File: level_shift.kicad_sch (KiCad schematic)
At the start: 37 parts, among them U1701 SN74LVC8T245PWR, U1702 SN74LVC8T245PWR, U1703 SN74LVC8T245PWR, U1704 SN74AVC4T245PWR, U1705 SN74AVC4T245PWR

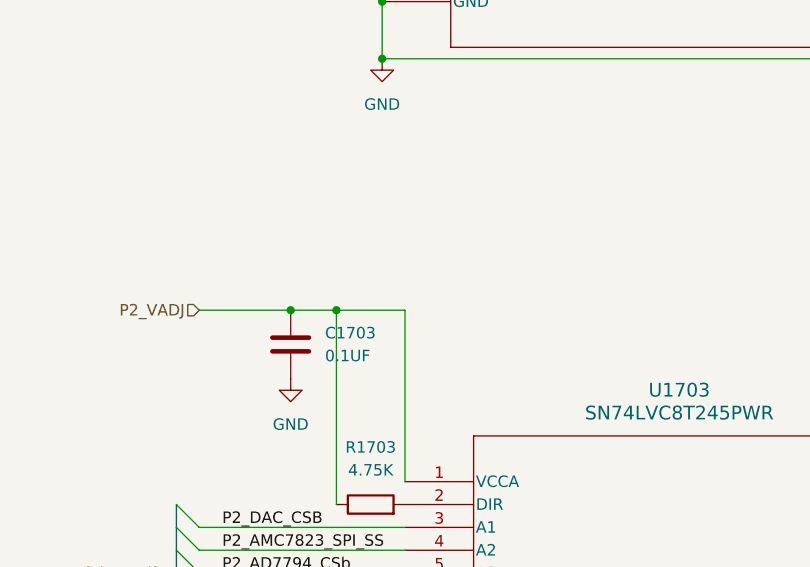
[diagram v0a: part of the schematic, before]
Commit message: Updates from Michal to fix ERC errors
Still lots of ERC warnings
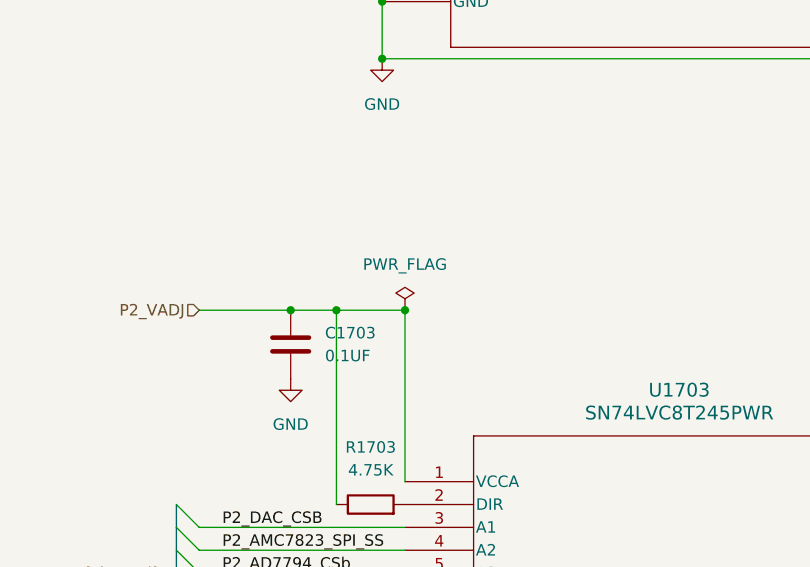
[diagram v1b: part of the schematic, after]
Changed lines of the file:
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@@
 	)
 	(junction
+		(at 67.31 191.77)
+		(diameter 0)
+		(color 0 0 0 0)
+	)
+	(junction
 		(at 172.72 236.22)
 		(diameter 0)
@@
 					(unit 1)
 				)
+			)
+		)
+	)
+	(symbol
+		(lib_id "power:PWR_FLAG")
+		(at 67.31 191.77 0)
+		(unit 1)
+		(exclude_from_sim no)
+		(in_bom yes)
+		(on_board yes)
+		(dnp no)
+		(fields_autoplaced yes)
+		(property "Reference" "#FLG06"
+			(at 67.31 189.865 0)
+			(effects
+				(font
+					(size 1.27 1.27)
+				)
+				(hide yes)
+			)
+		)
+		(property "Value" "PWR_FLAG"
+			(at 67.31 186.69 0)
+			(effects
+				(font
+					(size 1.27 1.27)
+				)
+			)
+		)
+		(property "Footprint" ""
+			(at 67.31 191.77 0)
+			(effects
+				(font
+					(size 1.27 1.27)
+				)
+				(hide yes)
+			)
+		)
+		(property "Datasheet" "~"
+			(at 67.31 191.77 0)
+			(effects
+				(font
+					(size 1.27 1.27)
+				)
+				(hide yes)
+			)
+		)
+		(property "Description" "Special symbol for telling ERC where power comes from"
+			(at 67.31 191.77 0)
+			(effects
+				(font
+					(size 1.27 1.27)
+				)
+				(hide yes)
+			)
+		)
+		(pin "1"
+		)
+		(instances
+			(project "zest"
+				(path "/00000000-0000-0000-0000-000000000003/00000000-0000-0000-0000-000000000014"
+					(reference "#FLG06")
+					(unit 1)
+				)

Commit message: Schematic Changes
Added Manufacturer/MPN/Description Fields to parts
Added libraries to project
Modified FMC schematic to use new symbol
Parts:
- C1701, C1702, C1703, C1704, C1705, C1706, C1707, C1708, C1709, C1710: Manufacturer (none) -> Murata; Manufacturer Part Number (none) -> GRM155R61A104KA01D
- R1701, R1702, R1703, R1704, R1705, R1706: Manufacturer (none) -> YAGEO; Manufacturer Part Number (none) -> RC0603FR-074K75L
- U1701, U1702, U1703: Manufacturer (none) -> Texas Instruments; Manufacturer Part Number (none) -> SN74LVC8T245PWR
- U1704, U1705: Manufacturer (none) -> Texas Instruments; Manufacturer Part Number (none) -> SN74AVC4T245PWR

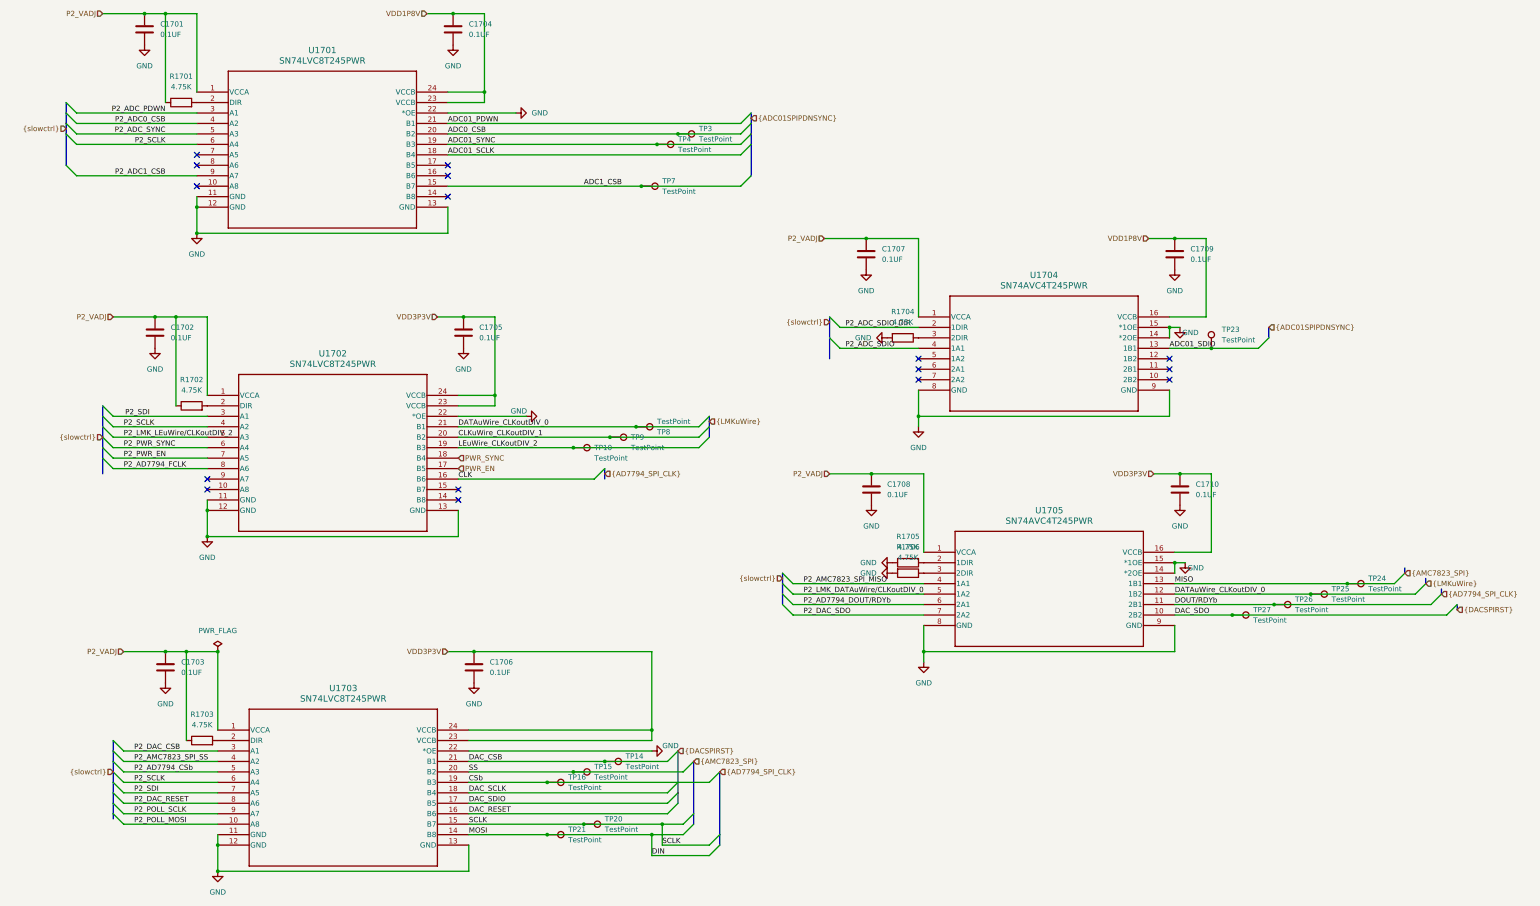
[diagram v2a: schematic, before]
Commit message: Schematics update
Cleaned up RF ADC and front end sections.
Verified that changes did not changes anything about the layout.
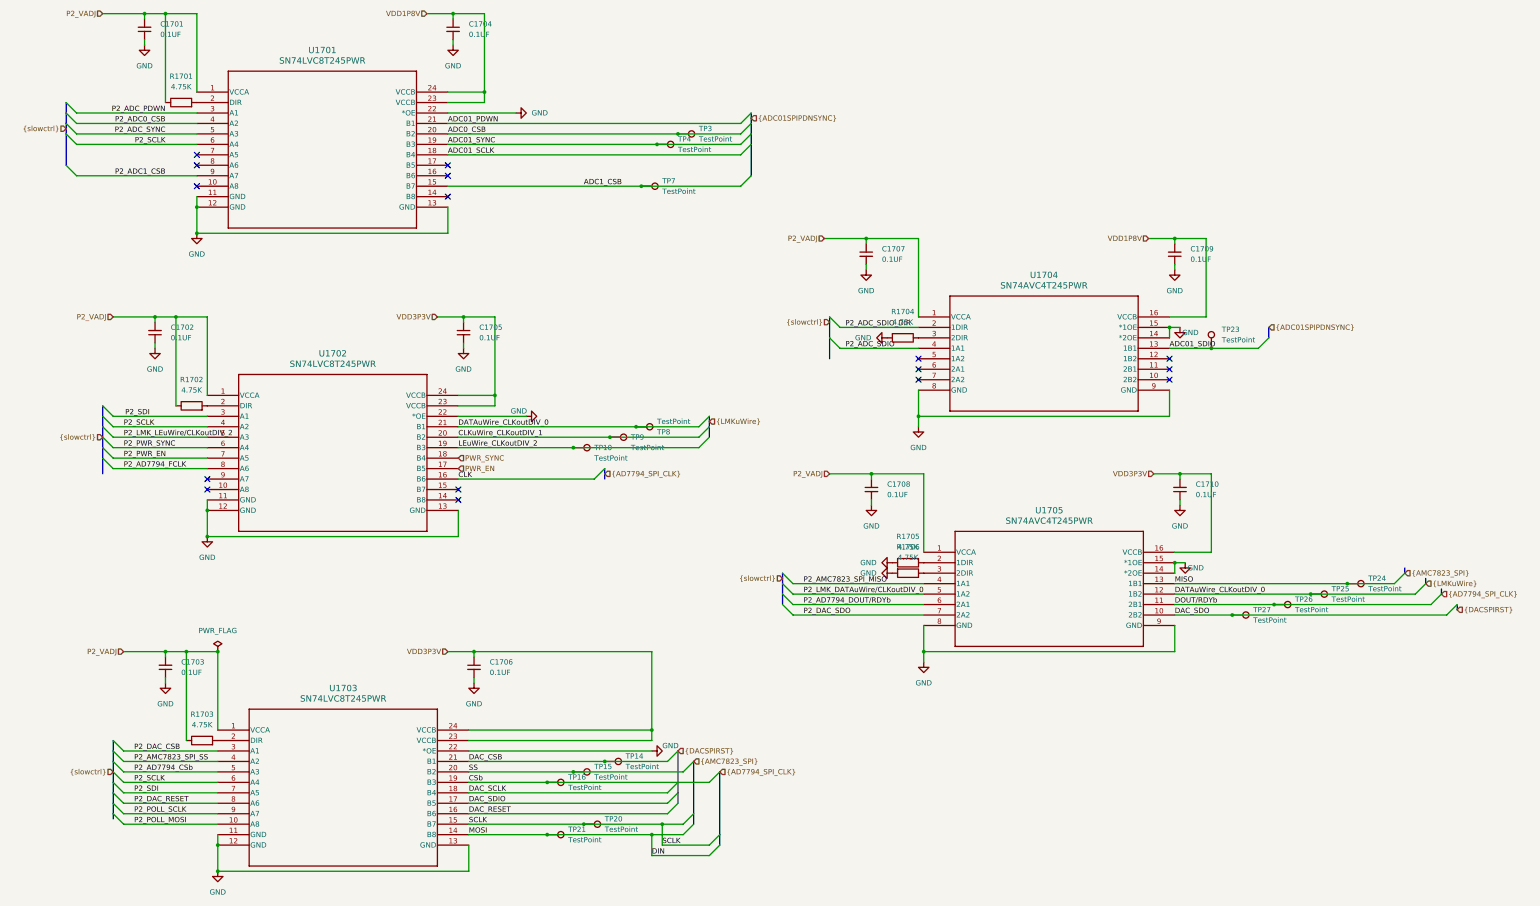
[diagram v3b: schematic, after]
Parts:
- C1701, C1702, C1703, C1704, C1705, C1706, C1707, C1708, C1709, C1710: symbol Device:C -> Device:C_Small
